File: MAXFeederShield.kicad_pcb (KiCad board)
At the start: 2 copper layers, 102 x 54 mm, 41 parts, among them J1 Conn_01x04_Male, J10 Conn_01x04_Male, J11 Conn_01x04_Male, J12 Conn_01x04_Male, J13 Conn_01x04_Male, J14 Conn_01x04_Male, J15 Conn_01x04_Male, J16 Conn_01x04_Male, J17 Conn_01x04_Male, J18 Conn_01x04_Male, J19 Conn_01x04_Male, J2 Barrel_Jack_Switch, J20 Conn_01x04_Male, J22 Conn_01x04_Male, J23 Conn_01x04_Male, J24 Conn_01x04_Male, J25 Conn_01x04_Male, J26 Conn_01x04_Male, J27 Conn_01x04_Male, J28 Conn_01x04_Male, J29 Conn_01x04_Male, J3 Conn_01x04_Male, J30 Conn_01x04_Male, J31 Conn_01x04_Male, J32 Conn_01x04_Male, J33 Conn_01x04_Male, J34 Conn_01x04_Male, J35 Conn_01x04_Male, J36 Conn_01x04_Male, J37 Screw_Terminal_01x02, J4 Conn_01x04_Male, J5 Conn_01x04_Male, J6 Conn_01x04_Male, J7 Conn_01x04_Male, J8 Conn_01x04_Male, J9 Conn_01x04_Male, SW1 SW_Push_Dual

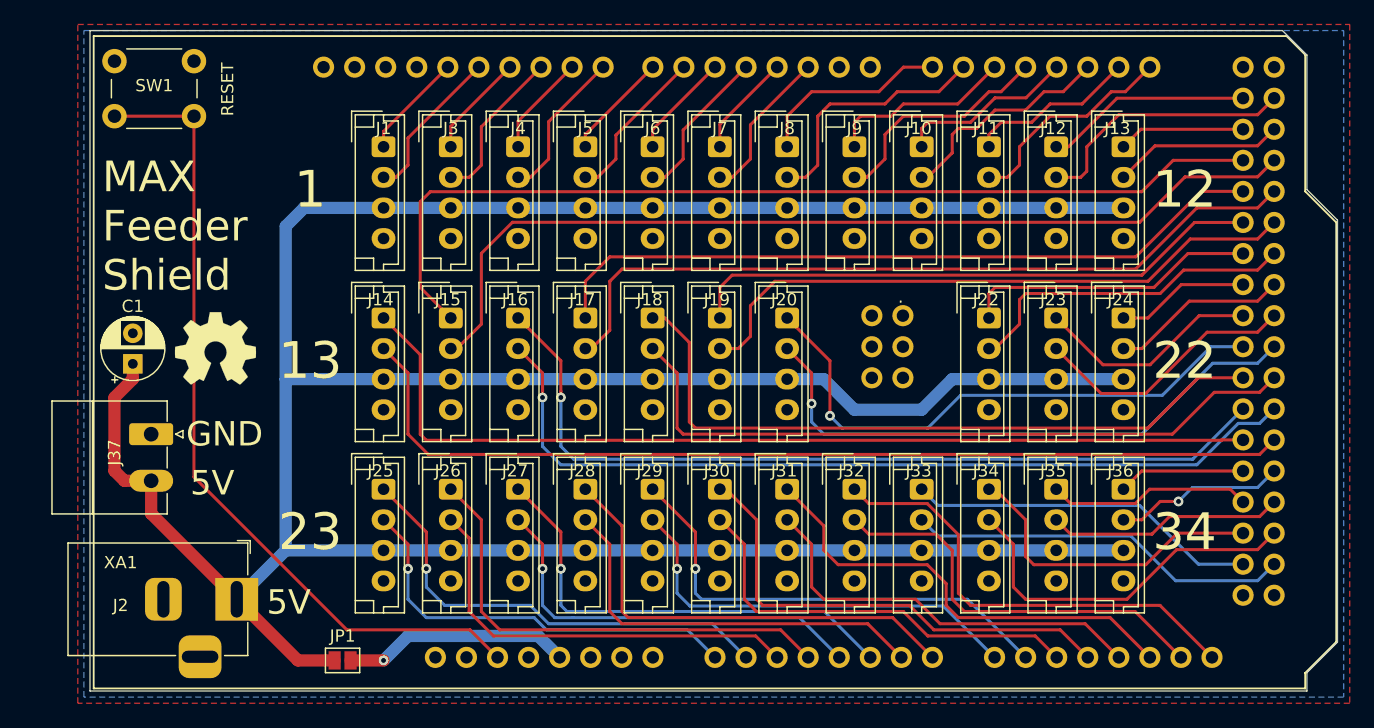
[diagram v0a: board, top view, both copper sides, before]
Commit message: Redesigned shield PCB, as well as adapter PCB, modified 0816 feeder firmware
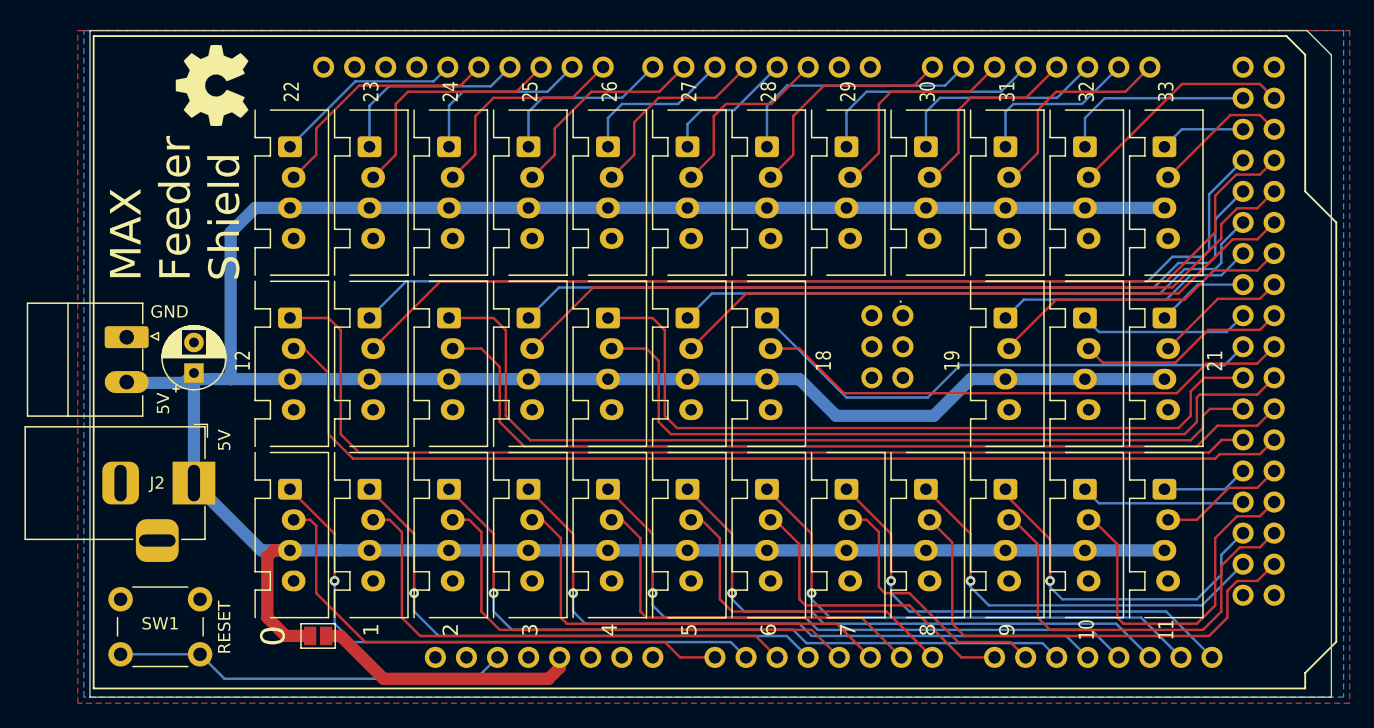
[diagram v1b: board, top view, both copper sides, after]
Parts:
- J1, J10, J11, J12, J13, J14, J15, J16, J17, J18, J19, J20, J22, J23, J24, J25, J26, J27, J28, J29, J3, J30, J31, J32, J33, J34, J35, J36, J4, J5, J6, J7, J8, J9: footprint Connector_JST:JST_EH_B4B-EH-A_1x04_P2.50mm_Vertical -> JST:JST_EH_B4B-EH-A_1x04_P2.50mm_Vertical_LOCKING
- moved SW1 44.0 mm to (82.0, 92.0)
- moved REF** 21.5 mm to (83.0, 45.5), turned to 90 degrees
- moved J2 10.1 mm to (81.5, 78.0)
- moved J37 8.25 mm to (76.0, 66.0)
- moved J1 7.50 mm to (89.5, 50.5)
- moved J14 7.50 mm to (89.5, 64.5)
- moved J25 7.50 mm to (89.5, 78.5)
- moved J15 6.50 mm to (96.0, 64.5)
- moved J26 6.50 mm to (96.0, 78.5)
- moved J3 6.50 mm to (96.0, 50.5)
- moved J16 5.50 mm to (102.5, 64.5)
- moved J27 5.50 mm to (102.5, 78.5)
- moved J4 5.50 mm to (102.5, 50.5)
- moved C1 5.06 mm to (81.5, 69.0)
- moved J17 4.50 mm to (109.0, 64.5)
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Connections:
- J10 pad 1: S8 -> F8
- J10 pad 2: F8 -> S8
- J8 pad 1: S6 -> F6
- J8 pad 2: F6 -> S6
- J9 pad 1: S7 -> F7
- J9 pad 2: F7 -> S7
- XA1 pad A10: S20 -> F30
- XA1 pad A11: F20 -> F19
- XA1 pad A12: S32 -> F31
- XA1 pad A13: F32 -> F20
- XA1 pad A14: S21 -> F32
- XA1 pad A5: F30 -> S19
- XA1 pad A6: S19 -> S31
- XA1 pad A7: F19 -> S20
- XA1 pad A8: S31 -> S32
- XA1 pad A9: F31 -> S21
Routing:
- net RESET: track 66.9 -> 32.4 mm
- net F30: track 38.0 -> 59.1 mm
- net F19: track 38.2 -> 55.1 mm, vias 0 -> 1
- net S21: track 33.7 -> 21.6 mm
- net F31: track 39.1 -> 50.9 mm
- net S34: track 19.4 -> 29.5 mm
- net F12: track 78.2 -> 87.9 mm
- net F29: track 38.0 -> 47.3 mm
- net S33: track 31.4 -> 39.7 mm
- net S32: track 33.8 -> 25.6 mm
- net S29: track 34.4 -> 42.3 mm, vias 1 -> 0
- net S12: track 79.8 -> 87.5 mm
- net F1: track 8.51 -> 16.1 mm
- net S20: track 34.8 -> 27.3 mm
- net S0: track 12.8 -> 20.1 mm
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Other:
- board size 102 x 54 mm -> 101.5 x 54.5 mm
- board text added: "0"
- board text added: "10"
- board text added: "11"
- board text added: "18"
- board text added: "19"
- board text added: "2"
- board text added: "21"
- board text added: "24"
- board text added: "25"
- board text added: "26"
- board text added: "27"
- board text added: "28"
- board text added: "29"
- board text added: "3"
- board text added: "30"
- board text added: "31"
- board text added: "32"
- board text added: "33"
- board text added: "4"
- board text added: "5"
- board text added: "6"
- board text added: "7"
- board text added: "8"
- board text added: "9"
- board text added: "FB"
- board text added: "SERVO"
- board text removed: "13"
- board text removed: "34"

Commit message: tweaked pad size on PCB and added 3d files for 8mm feeder
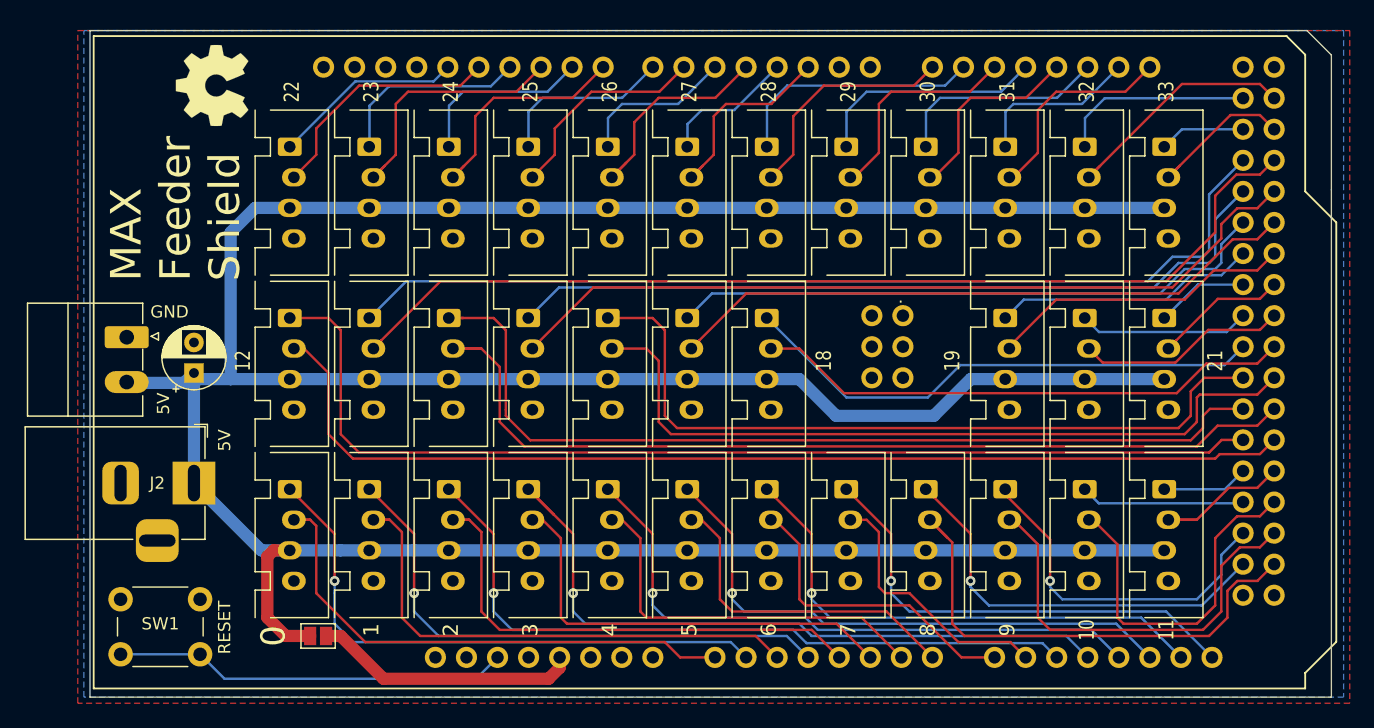
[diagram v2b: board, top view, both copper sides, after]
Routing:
- net F19: track 55.1 -> 58.1 mm
- net S23: track 10.3 -> 12.7 mm
- net S13: track 74.4 -> 76.7 mm
- net S33: track 39.7 -> 41.7 mm
- net S4: track 16.3 -> 17.9 mm
- net S30: track 40.1 -> 41.4 mm
- net S29: track 42.3 -> 43.7 mm
- net S18: track 41.8 -> 43.1 mm
- net S5: track 15.1 -> 16.4 mm
- net S2: track 17.9 -> 19.2 mm
- net S11: track 11.3 -> 12.6 mm
- net S1: track 19.9 -> 21.2 mm
- net S10: track 18.8 -> 20.1 mm
- net F13: track 74.8 -> 76.0 mm
- net S26: track 51.9 -> 52.9 mm
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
